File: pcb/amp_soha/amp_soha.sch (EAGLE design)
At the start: 55 parts, among them IC1 7812, IC2 7912, IC3 OPA2134PA, Q1 J113, Q2 J113, Q3 J113, Q4 J113, U1 TROCAR

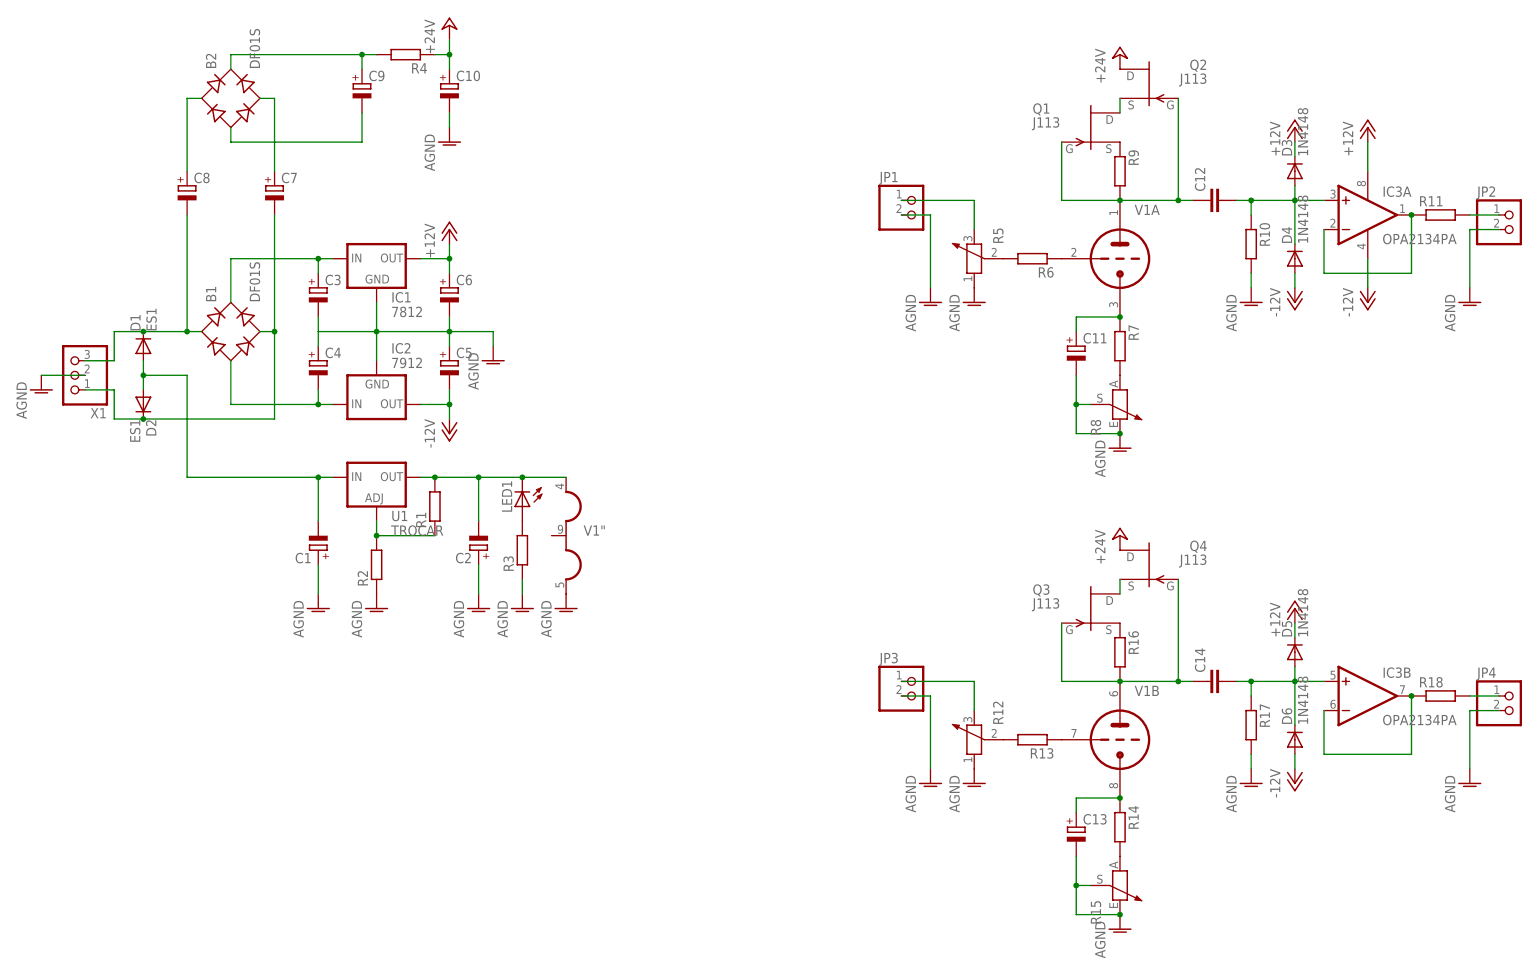
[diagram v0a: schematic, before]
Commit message: 
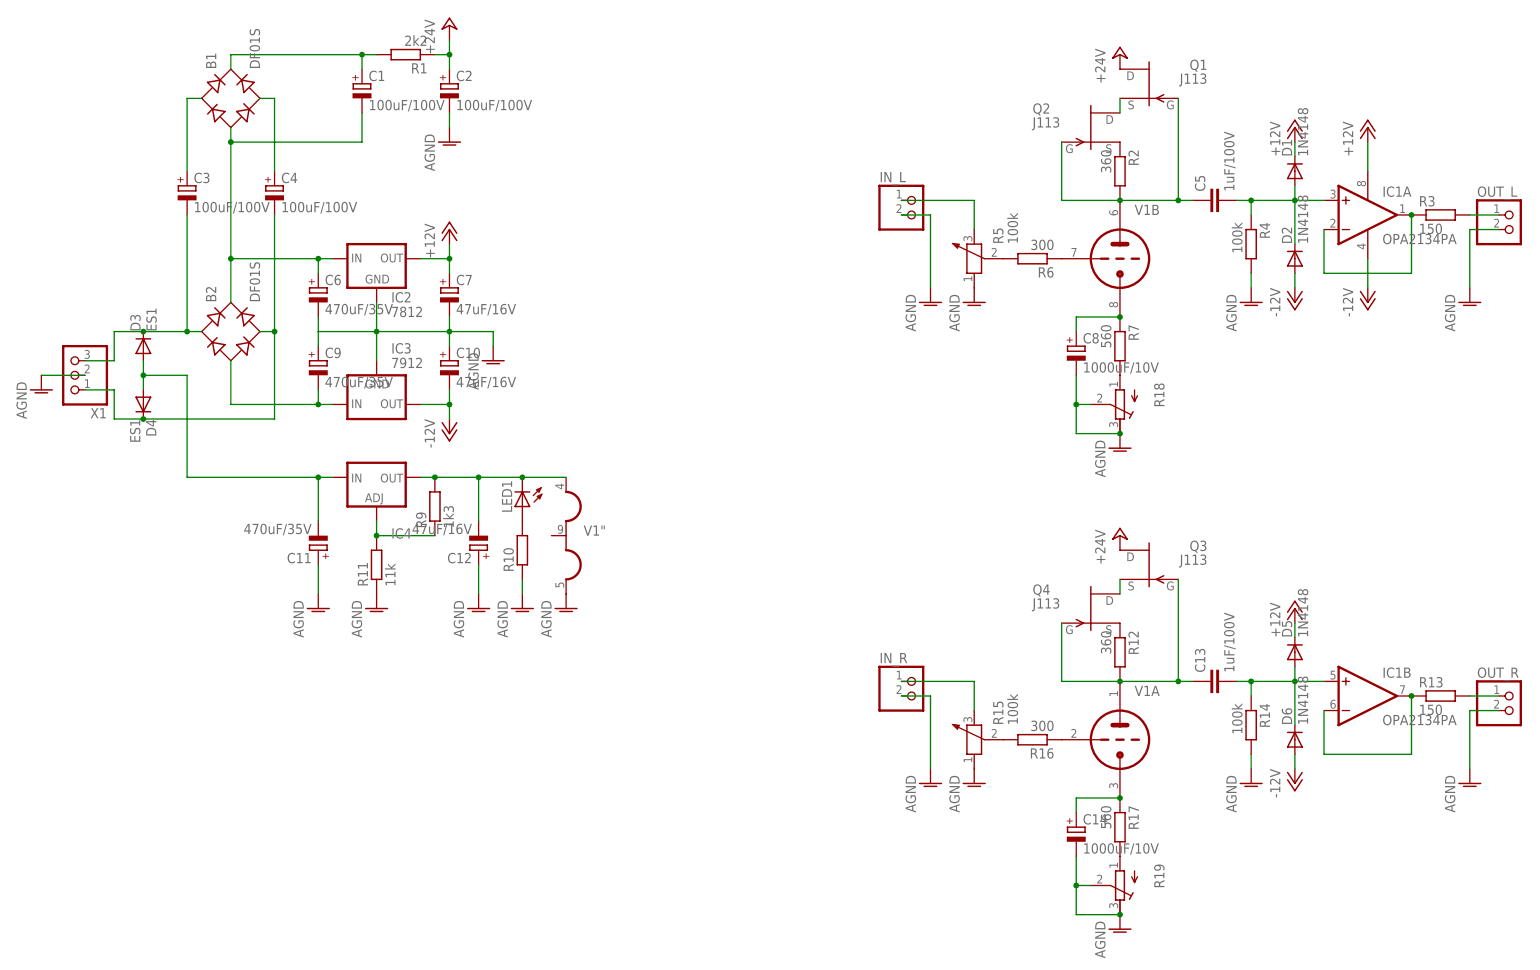
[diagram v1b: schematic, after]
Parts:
- removed R8: (no value), amp_soha:POTENTIOMETER_CT6
- removed U1: TROCAR, amp_soha:V_REG_317
- added IC4: (no value), amp_soha:LM337TS
- added R19: (no value), amp_soha:RTRIM329Y
- C1, C2, C3, C4: value (none) -> 100uF/100V
- C10, C7: value (none) -> 47uF/16V; device amp_soha:CPOL-EUE5-10,5 -> amp_soha:CPOL-EUE2.5-6
- C11, C6, C9: value (none) -> 470uF/35V
- C12: value (none) -> 47uF/16V; device amp_soha:C-EU102-043X133 -> amp_soha:CPOL-EUE2.5-6
- C13, C5: value (none) -> 1uF/100V; device amp_soha:CPOL-EUE5-10,5 -> amp_soha:C-EU150-072X183
- C14: value (none) -> 1000uF/10V; device amp_soha:C-EU102-043X133 -> amp_soha:CPOL-EUE5-10,5
- C8: value (none) -> 1000uF/10V
- D1, D2: value ES1 -> 1N4148; device amp_soha:ES1 -> amp_soha:1N4148
- D3, D4: value 1N4148 -> ES1; device amp_soha:1N4148 -> amp_soha:ES1
- IC1: value 7812 -> OPA2134PA; device amp_soha:78XXTO-220 -> amp_soha:OPA2134PA
- IC2: value 7912 -> 7812; device amp_soha:79XXTO-220 -> amp_soha:78XXTO-220
- IC3: value OPA2134PA -> 7912; device amp_soha:OPA2134PA -> amp_soha:79XXTO-220
- R1: value (none) -> 2k2
- R11: value (none) -> 11k
- R12: value (none) -> 360; device amp_soha:POTENTIOMETER_ -> amp_soha:R-EU_
- R13, R3: value (none) -> 150
- R14, R4, R5: value (none) -> 100k
- R15: value (none) -> 100k; device amp_soha:POTENTIOMETER_CT6 -> amp_soha:POTENTIOMETER_
- R16, R6: value (none) -> 300
- R17, R7: value (none) -> 560
- R18: device amp_soha:R-EU_ -> amp_soha:RTRIM329Y
- R2: value (none) -> 360
- R9: value (none) -> 1k3
- renumbered JP1 to IN_L, JP2 to OUT_L, JP3 to IN_R, JP4 to OUT_R
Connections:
- removed net N$30: R14.2, R15.1
- net +12V: now also C7.+, D1.C, IC1A.V+, IC2.OUT; no longer C6.+, D3.C, IC1.OUT, IC3A.V+
- net +24V: now also C2.+, Q1.D, Q3.D, R1.1; no longer C10.+, Q2.D, Q4.D, R4.1
- net -12.6V: now also C12.-, IC4.OUT, R9.2; no longer C2.-, R1.2, U1.OUT
- net -12V: now also C10.-, D2.A, IC1A.V-, IC3.OUT; no longer C5.-, D4.A, IC2.OUT, IC3A.V-
- net AGND: now also C10.+, C11.+, C12.+, C14.-, C2.-, C7.-, C8.-, C9.+, IC3.GND, R10.1, R11.1, R14.2, R15.1, R18.E, R18.S, R19.E, R19.S, R4.2; no longer C1.+, C10.-, C11.-, C13.-, C2.+, C3.-, C4.+, C5.+, IC1.GND, R10.2, R12.1, R15.2, R15.3, R17.2, R2.1, R3.1, R8.2, R8.3
- net N$1: now also B2.AC1, C3.-, D3.C; no longer B1.AC1, C8.-, D1.C
- net N$10: now also R16.1, V1A.TG; no longer B2.-, C9.-
- net N$11: now also B1.+, C1.+, R1.2; no longer B2.+, C9.+, R4.2
- net N$14: now also V1B.TG; no longer V1A.TG
- net N$15: now also C8.+, V1B.TK; no longer C11.+, V1A.TK
- net N$16: now also Q2.S, R2.1; no longer Q1.S, R9.1
- net N$17: now also R18.A; no longer R8.1
- net N$18: now also R17.2, R19.A; no longer R13.1, V1B.TG
- net N$19: now also C5.1, R2.2, V1B.TA; no longer C12.1, R9.2, V1A.TA
- net N$2: now also B2.AC2, C4.-, D4.C; no longer B1.AC2, C7.-, D2.C
- net N$20: now also Q1.S, Q2.D; no longer Q1.D, Q2.S
- net N$22: now also C5.2, D1.A, D2.C, IC1A.+IN, R4.1; no longer C12.2, D3.A, D4.C, IC3A.+IN, R10.1
- net N$24: now also IC1A.-IN, IC1A.OUT, R3.1; no longer IC3A.-IN, IC3A.OUT, R11.1
- net N$25: now also R3.2; no longer R11.2
- net N$26: now also R15.2; no longer R12.2
- net N$27: now also R15.3, R16.2; no longer R12.3, R13.2
- net N$29: now also C14.+, R17.1, V1A.TK; no longer C13.+, R14.1, V1B.TK
- net N$3: now also C11.-, D3.A, D4.A, IC4.IN; no longer C1.-, D1.A, D2.A, U1.IN
- net N$31: now also C13.1, R12.2, V1A.TA; no longer C14.1, R16.2, V1B.TA
- net N$32: now also Q4.S, R12.1; no longer Q3.S, R16.1
- net N$33: now also Q3.S, Q4.D; no longer Q3.D, Q4.S
- net N$34: now also C13.2, IC1B.+IN, R14.1; no longer C14.2, IC3B.+IN, R17.1
- net N$35: now also IC1B.-IN, IC1B.OUT, R13.1; no longer IC3B.-IN, IC3B.OUT, R18.1
- net N$36: now also R13.2; no longer R18.2
- net N$4: now also IC4.ADJ, R11.2, R9.1; no longer R1.1, R2.2, U1.ADJ
- net N$5: now also B2.-, C9.-, IC3.IN; no longer B1.-, C4.-, IC2.IN
- net N$6: now also B1.-, B2.+, C1.-, C6.+, IC2.IN; no longer B1.+, C3.+, IC1.IN
- net N$7: now also R10.2; no longer R3.2
- net N$8: now also B1.AC1, C3.+; no longer B2.AC1, C8.+
- net N$9: now also B1.AC2, C4.+; no longer B2.AC2, C7.+
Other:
- moved on the sheet: B1, B2, C1, C10, C11, C2, C3, C4, C6, C7, C8, C9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

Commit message: 
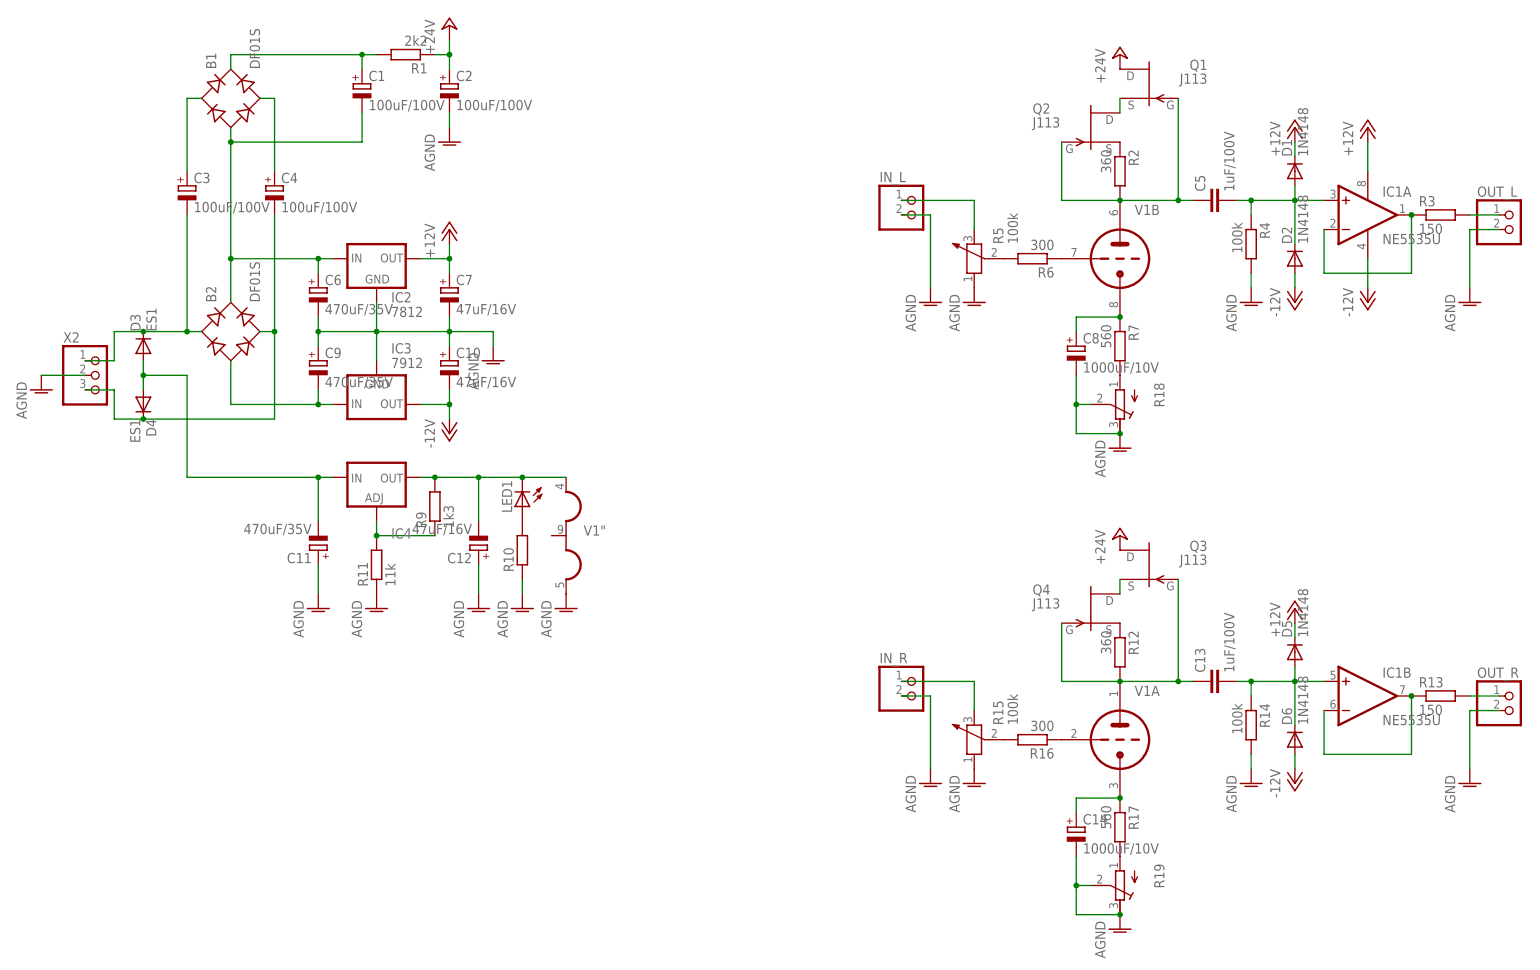
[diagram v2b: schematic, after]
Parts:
- removed X1: (no value), amp_soha:W237-103
- added X2: (no value), amp_soha:W237-103
- IC1: value OPA2134PA -> NE5535U; device amp_soha:OPA2134PA -> amp_soha:NE5535U
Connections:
- net AGND: now also X2.2; no longer X1.2
- net N$1: now also X2.1; no longer X1.3
- net N$2: now also X2.3; no longer X1.1
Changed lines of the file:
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@@
 </classes>
 <parts>
-<part name="X1" library="amp_soha" deviceset="W237-103" device=""/>
 <part name="B2" library="amp_soha" deviceset="DF*S" device="" technology="01"/>
 <part name="D3" library="amp_soha" deviceset="ES1" device=""/>
@@
 <part name="C5" library="amp_soha" deviceset="C-EU" device="150-072X183" value="1uF/100V"/>
 <part name="P+3" library="amp_soha" deviceset="+24V" device=""/>
-<part name="IC1" library="amp_soha" deviceset="OPA2*" device="PA" technology="134"/>
+<part name="IC1" library="amp_soha" deviceset="NE5535" device="U"/>
 <part name="P-2" library="amp_soha" deviceset="-12V" device=""/>
 <part name="P+4" library="amp_soha" deviceset="+12V" device=""/>
@@
 <part name="R19" library="amp_soha" deviceset="RTRIM329" device="Y"/>
 <part name="R18" library="amp_soha" deviceset="RTRIM329" device="Y"/>
+<part name="X2" library="amp_soha" deviceset="W237-103" device=""/>
 </parts>
 <sheets>
@@
 </plain>
 <instances>
-<instance part="X1" gate="G$1" x="2.54" y="17.78" rot="R180"/>
 <instance part="B2" gate="G$1" x="30.48" y="25.4" rot="R90"/>
 <instance part="D3" gate="G$1" x="15.24" y="22.86" rot="R90"/>
@@
 <instance part="R19" gate="G$1" x="185.42" y="-71.12" rot="R180"/>
 <instance part="R18" gate="G$1" x="185.42" y="12.7" rot="R180"/>
+<instance part="X2" gate="G$1" x="7.62" y="17.78"/>
 </instances>
 <busses>
@@
 <net name="AGND" class="0">
 <segment>
-<pinref part="X1" gate="G$1" pin="2"/>
 <pinref part="AGND1" gate="VR1" pin="AGND"/>
 <wire x1="5.08" y1="17.78" x2="-2.54" y2="17.78" width="0.1524" layer="91"/>
+<pinref part="X2" gate="G$1" pin="2"/>
 </segment>
 <segment>
@@
 <wire x1="68.58" y1="25.4" x2="76.2" y2="25.4" width="0.1524" layer="91"/>
 <wire x1="76.2" y1="25.4" x2="76.2" y2="22.86" width="0.1524" layer="91"/>
+<junction x="45.72" y="25.4"/>
 </segment>
 <segment>
@@
 <net name="N$1" class="0">
 <segment>
-<pinref part="X1" gate="G$1" pin="3"/>
 <wire x1="5.08" y1="20.32" x2="10.16" y2="20.32" width="0.1524" layer="91"/>
 <wire x1="10.16" y1="20.32" x2="10.16" y2="25.4" width="0.1524" layer="91"/>
@@
 <pinref part="C3" gate="G$1" pin="-"/>
 <wire x1="22.86" y1="45.72" x2="22.86" y2="25.4" width="0.1524" layer="91"/>
+<pinref part="X2" gate="G$1" pin="1"/>
 </segment>
 </net>
 <net name="N$2" class="0">
 <segment>
-<pinref part="X1" gate="G$1" pin="1"/>
 <wire x1="5.08" y1="15.24" x2="10.16" y2="15.24" width="0.1524" layer="91"/>
 <wire x1="10.16" y1="15.24" x2="10.16" y2="10.16" width="0.1524" layer="91"/>
@@
 <pinref part="C4" gate="G$1" pin="-"/>
 <wire x1="38.1" y1="45.72" x2="38.1" y2="25.4" width="0.1524" layer="91"/>
+<pinref part="X2" gate="G$1" pin="3"/>
 </segment>
 </net>
